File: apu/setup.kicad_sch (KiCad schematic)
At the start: 22 parts, among them U1 X818336-001

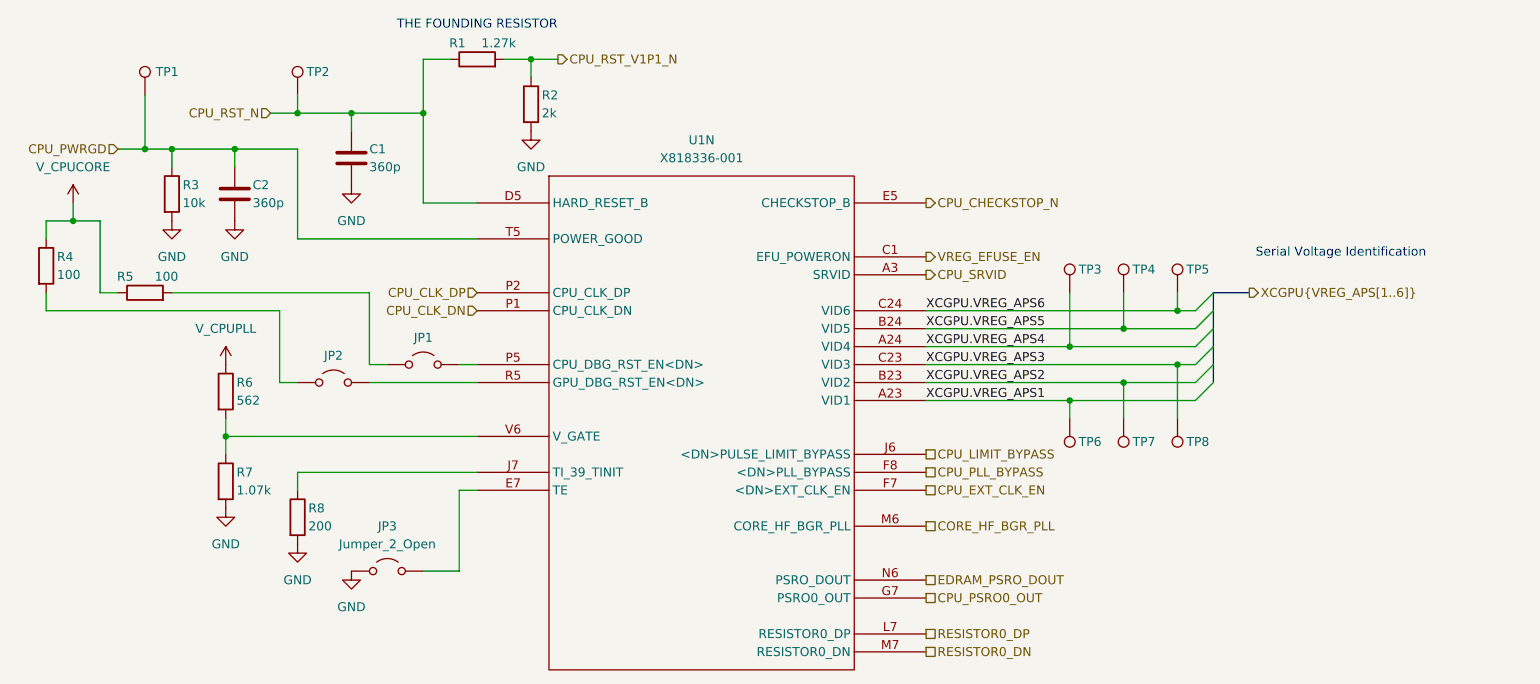
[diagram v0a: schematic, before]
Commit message: Cleanup, SMC GPIO connections and Temperature sensing
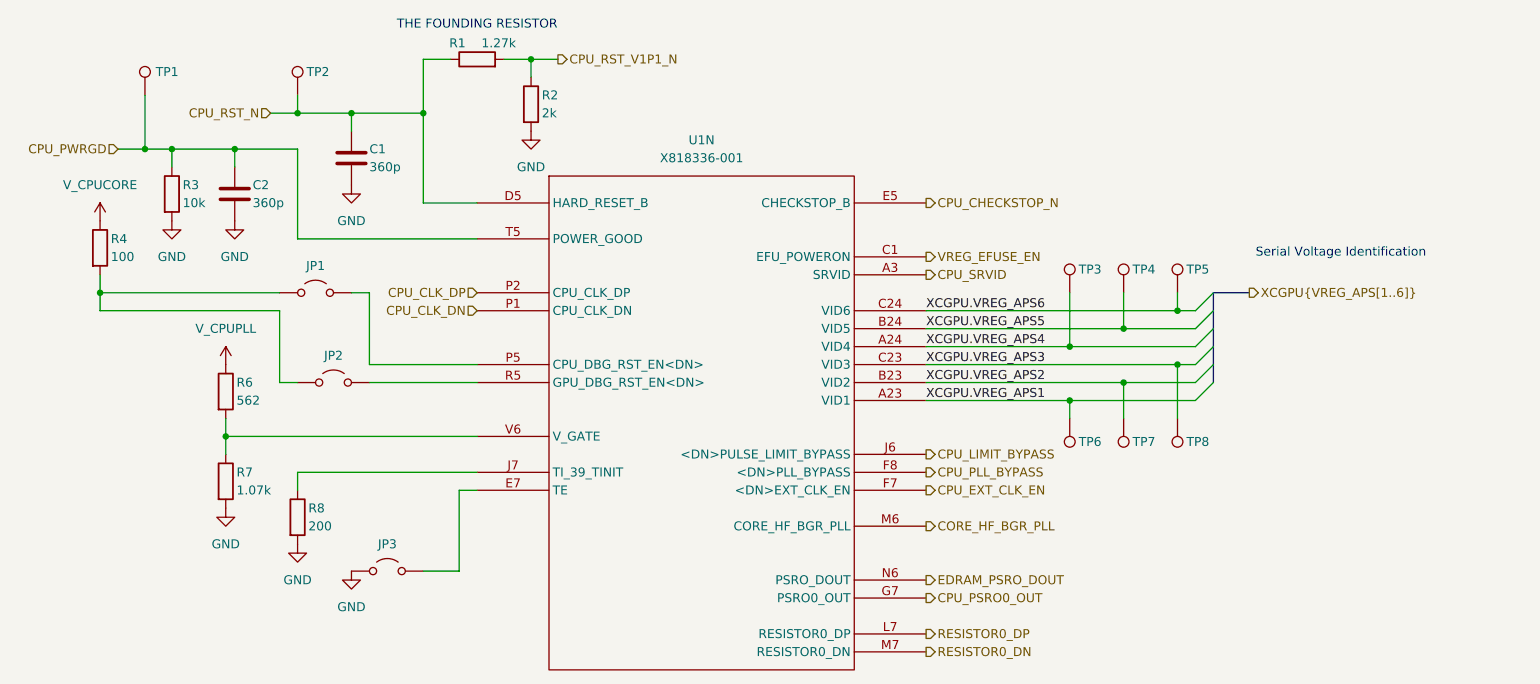
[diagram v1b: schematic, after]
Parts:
- removed R5: 100, symbol Device:R
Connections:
- net at JP2.1 (A), R4.2: now also JP1.1 (A)
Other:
- moved on the sheet: JP1, R4

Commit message: Internal Connectors
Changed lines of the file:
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@@
 	(text "Serial Voltage Identification\n"
 		(exclude_from_sim no)
-		(at 240.284 70.612 0)
+		(at 237.744 72.644 0)
 		(effects
 			(font
@@
 	(bus
 		(pts
-			(xy 222.25 76.2) (xy 227.33 76.2)
+			(xy 222.25 76.2) (xy 224.79 76.2)
 		)
 		(stroke
@@
 	(hierarchical_label "XCGPU{VREG_APS[1..6]}"
 		(shape output)
-		(at 227.33 76.2 0)
-		(effects
-			(font
+		(at 224.79 76.2 0)
+		(effects
+			(font

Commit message: Cleanup & Debug I/O
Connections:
- net V_CPUPLL renamed +1.8V
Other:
- note added: "VID (Voltage Identification Definition)"
- note removed: "Serial Voltage Identification"
- moved on the sheet: C2, JP3, R2, TP1

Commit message: Debug Connectors
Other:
- moved on the sheet: JP1
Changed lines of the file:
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@@
 	)
 	(junction
-		(at 64.77 76.2)
-		(diameter 0)
-		(color 0 0 0 0)
-	)
-	(junction
 		(at 85.09 55.88)
 		(diameter 0)
@@
 	)
 	(junction
+		(at 90.17 81.28)
+		(diameter 0)
+		(color 0 0 0 0)
+	)
+	(junction
 		(at 92.71 50.8)
 		(diameter 0)
@@
 	(wire
 		(pts
-			(xy 64.77 73.66) (xy 64.77 76.2)
+			(xy 64.77 73.66) (xy 64.77 78.74)
 		)
 		(stroke
@@
 	(wire
 		(pts
-			(xy 100.33 76.2) (xy 102.87 76.2)
+			(xy 92.71 101.6) (xy 92.71 104.14)
 		)
 		(stroke
@@
 	(wire
 		(pts
-			(xy 92.71 101.6) (xy 92.71 104.14)
+			(xy 100.33 50.8) (xy 110.49 50.8)
 		)
 		(stroke
@@
 	(wire
 		(pts
-			(xy 100.33 50.8) (xy 110.49 50.8)
+			(xy 74.93 55.88) (xy 85.09 55.88)
 		)
 		(stroke
@@
 	(wire
 		(pts
-			(xy 74.93 55.88) (xy 85.09 55.88)
+			(xy 85.09 55.88) (xy 85.09 58.42)
 		)
 		(stroke
@@
 	(wire
 		(pts
-			(xy 85.09 55.88) (xy 85.09 58.42)
+			(xy 85.09 55.88) (xy 95.25 55.88)
 		)
 		(stroke
@@
 	(wire
 		(pts
-			(xy 102.87 76.2) (xy 102.87 86.36)
+			(xy 82.55 93.98) (xy 82.55 96.52)
 		)
 		(stroke
@@
 	(wire
 		(pts
-			(xy 85.09 55.88) (xy 95.25 55.88)
+			(xy 209.55 81.28) (xy 219.71 81.28)
 		)
 		(stroke
@@
 	(wire
 		(pts
-			(xy 82.55 93.98) (xy 82.55 96.52)
+			(xy 92.71 50.8) (xy 100.33 50.8)
 		)
 		(stroke
@@
 	(wire
 		(pts
-			(xy 209.55 81.28) (xy 219.71 81.28)
+			(xy 90.17 81.28) (xy 90.17 88.9)
 		)
 		(stroke
@@
 	(wire
 		(pts
-			(xy 92.71 50.8) (xy 100.33 50.8)
+			(xy 74.93 50.8) (xy 74.93 55.88)
 		)
 		(stroke
@@
 	(wire
 		(pts
-			(xy 74.93 50.8) (xy 74.93 55.88)
+			(xy 102.87 81.28) (xy 105.41 81.28)
 		)
 		(stroke
@@
 	(wire
 		(pts
-			(xy 102.87 86.36) (xy 118.11 86.36)
+			(xy 105.41 81.28) (xy 105.41 86.36)
 		)
 		(stroke
@@
 	(wire
 		(pts
-			(xy 92.71 88.9) (xy 90.17 88.9)
+			(xy 105.41 86.36) (xy 118.11 86.36)
 		)
 		(stroke
@@
 	(wire
 		(pts
-			(xy 219.71 86.36) (xy 217.17 86.36)
+			(xy 92.71 88.9) (xy 90.17 88.9)
 		)
 		(stroke
@@
 	(wire
 		(pts
-			(xy 110.49 43.18) (xy 114.3 43.18)
+			(xy 219.71 86.36) (xy 217.17 86.36)
 		)
 		(stroke
@@
 	(wire
 		(pts
-			(xy 64.77 76.2) (xy 90.17 76.2)
+			(xy 110.49 43.18) (xy 114.3 43.18)
 		)
 		(stroke
@@
 	(wire
 		(pts
-			(xy 90.17 78.74) (xy 90.17 88.9)
+			(xy 90.17 78.74) (xy 90.17 81.28)
 		)
 		(stroke
@@
 	(wire
 		(pts
+			(xy 90.17 81.28) (xy 92.71 81.28)
+		)
+		(stroke
+			(width 0)
+			(type default)
+		)
+	)
+	(wire
+		(pts
 			(xy 219.71 78.74) (xy 217.17 78.74)
 		)
@@
 	(wire
 		(pts
-			(xy 64.77 76.2) (xy 64.77 78.74)
-		)
-		(stroke
-			(width 0)
-			(type default)
-		)
-	)
-	(wire
-		(pts
 			(xy 82.55 96.52) (xy 82.55 99.06)
 		)
@@
 	(symbol
 		(lib_id "Jumper:Jumper_2_Open")
-		(at 95.25 76.2 0)
+		(at 97.79 81.28 0)
 		(unit 1)
 		(exclude_from_sim no)
@@
 		(dnp no)
 		(property "Reference" "JP1"
-			(at 95.25 72.39 0)
+			(at 97.79 77.47 0)
 			(effects
 				(font
@@
 		)
 		(property "Value" "Jumper_2_Open"
-			(at 95.25 72.39 0)
+			(at 97.79 77.47 0)
 			(effects
 				(font
@@
 		)
 		(property "Footprint" ""
-			(at 95.25 76.2 0)
+			(at 97.79 81.28 0)
 			(effects
 				(font
@@
 		)
 		(property "Datasheet" "~"
-			(at 95.25 76.2 0)
+			(at 97.79 81.28 0)
 			(effects
 				(font
@@
 		)
 		(property "Description" "Jumper, 2-pole, open"
-			(at 95.25 76.2 0)
+			(at 97.79 81.28 0)
 			(effects
 				(font

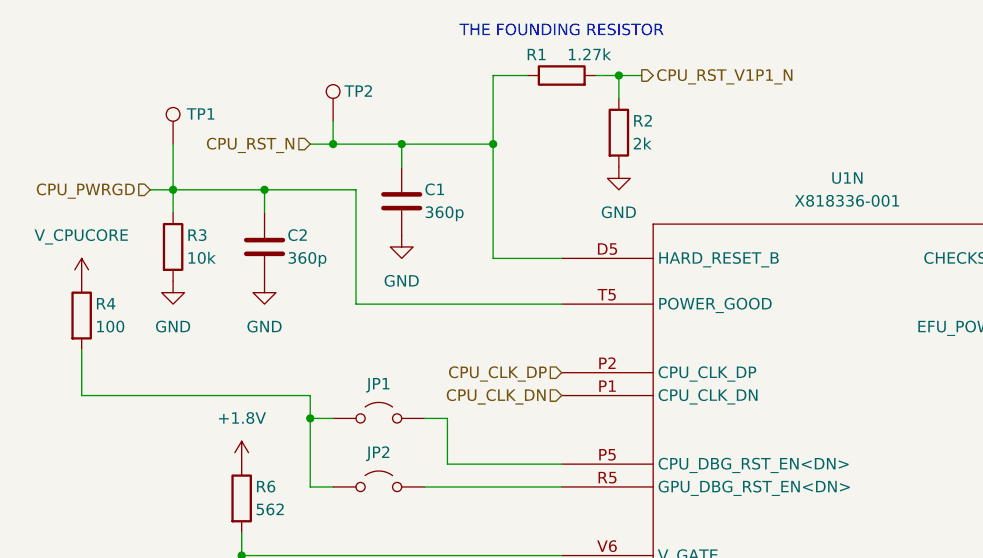
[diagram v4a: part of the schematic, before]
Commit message: Nand Flash, Sata Connectors and removing (hopefully) unnecessary things
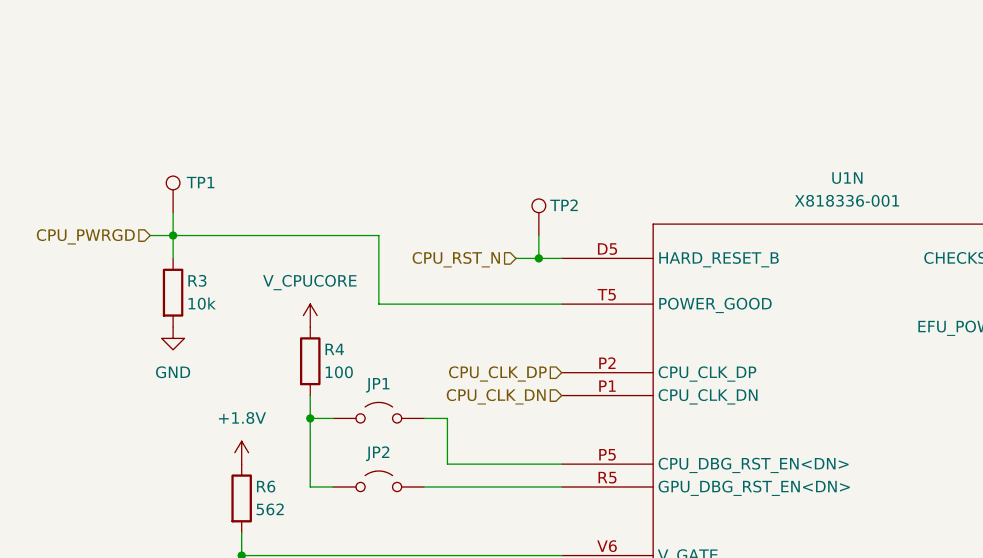
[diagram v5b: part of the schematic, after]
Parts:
- removed C1, C2: 360p, symbol Device:C
- removed R1: 1.27k, symbol Device:R
- removed R2: 2k, symbol Device:R
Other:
- note removed: "THE FOUNDING RESISTOR"
- moved on the sheet: R3, R4, TP1, TP2

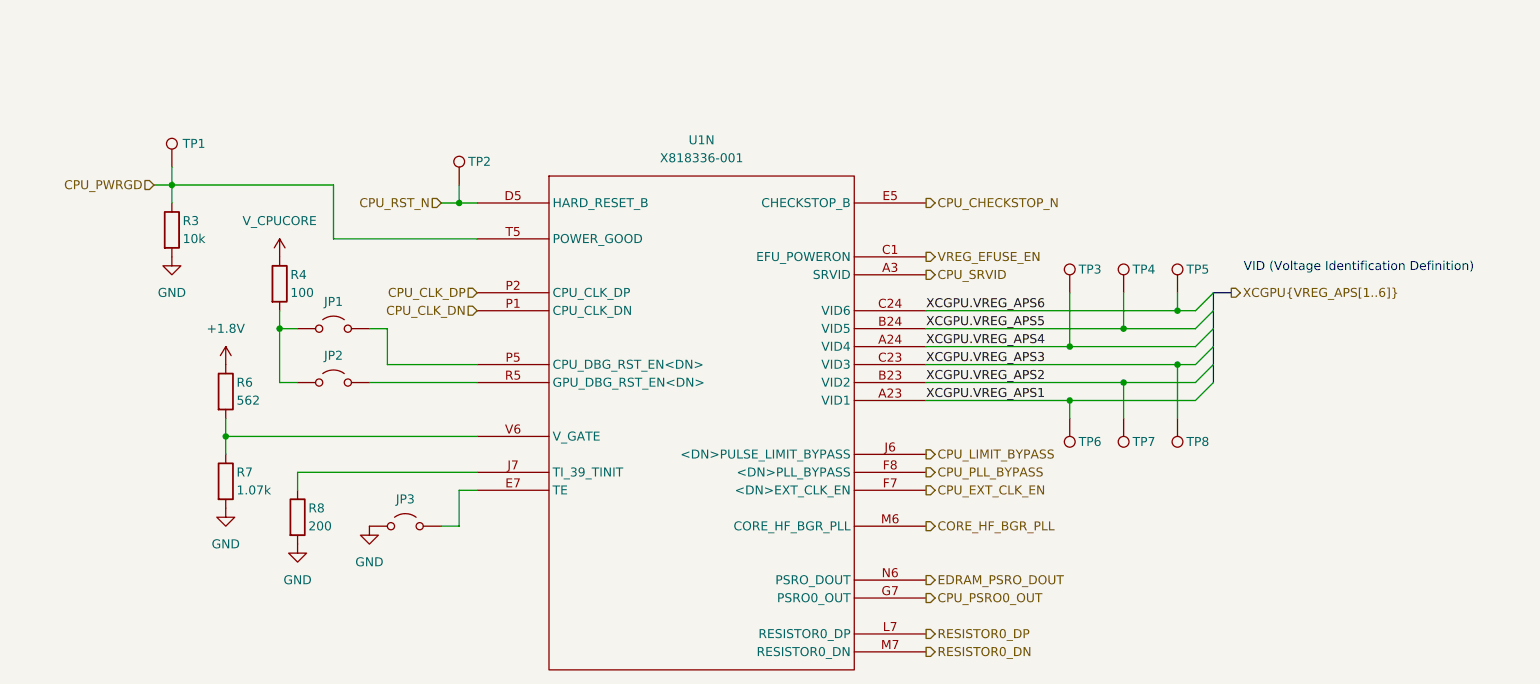
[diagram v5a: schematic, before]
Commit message: Multipurpose and standby power rails, Reannotated schematic
Added V_1P2, V_1P8, V_5P0DUAL, V_EFUSE, V_GPUPCIE, V_3P3STBY and V_1P2STBY
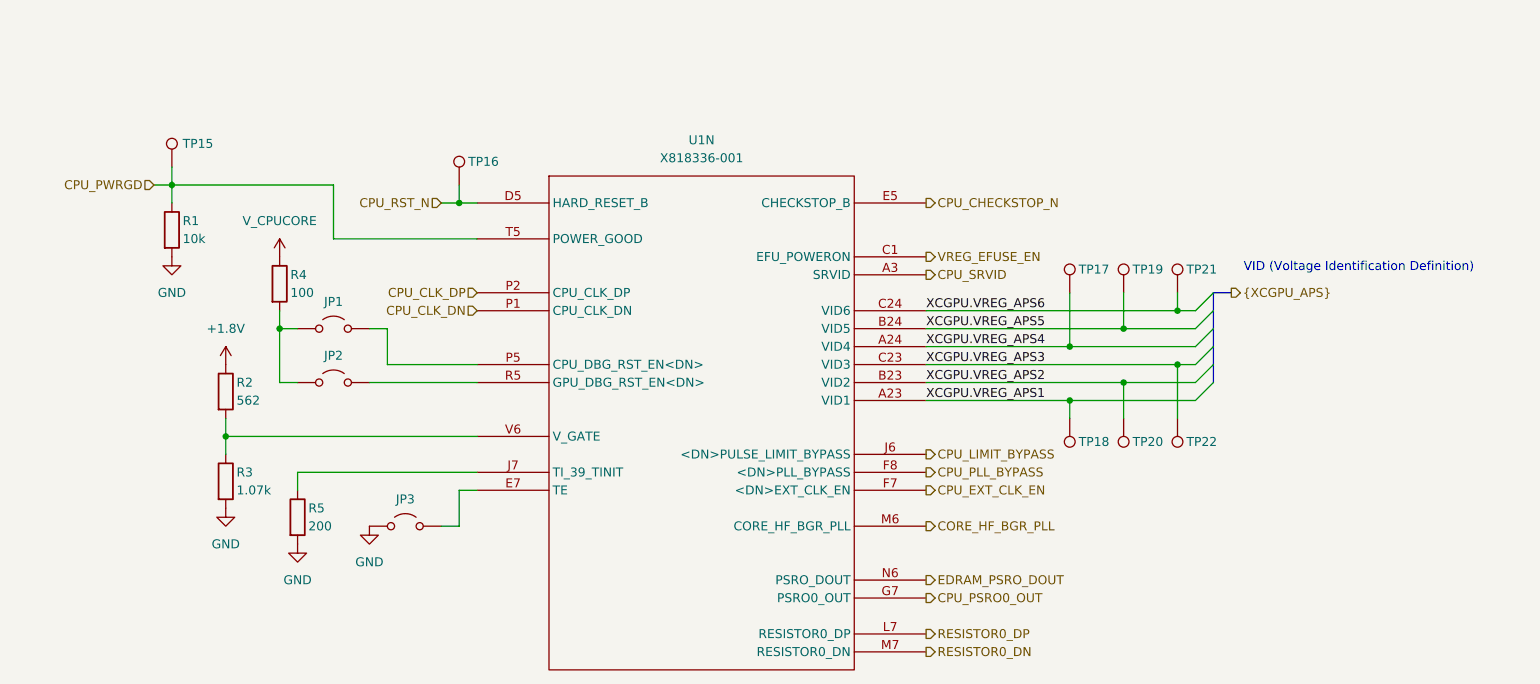
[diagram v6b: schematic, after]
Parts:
- renumbered R3 to R1, R6 to R2, R7 to R3, R8 to R5, TP1 to TP15, TP2 to TP16, TP3 to TP17, TP6 to TP18, TP4 to TP19, TP7 to TP20, TP5 to TP21, TP8 to TP22
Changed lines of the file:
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@@
 		)
 	)
-	(hierarchical_label "XCGPU{VREG_APS[1..6]}"
+	(hierarchical_label "{XCGPU_APS}"
 		(shape output)
 		(at 224.79 76.2 0)
@@
 		(on_board yes)
 		(dnp no)
-		(property "Reference" "TP2"
+		(property "Reference" "TP16"
 			(at 116.84 57.658 0)
 			(effects
@@
 			(project "StingBurst"
 				(path "/16640ecb-e4a4-4594-871b-70047bfba6e0/15d9acf0-ed9b-44aa-a266-2c44722c6abb/ae60d6be-3587-4435-b525-992ac09fdec2"
-					(reference "TP2")
+					(reference "TP16")
 					(unit 1)
 				)
@@
 		(on_board yes)
 		(dnp no)
-		(property "Reference" "TP5"
+		(property "Reference" "TP21"
 			(at 218.44 72.898 0)
 			(effects
@@
 			(project "StingBurst"
 				(path "/16640ecb-e4a4-4594-871b-70047bfba6e0/15d9acf0-ed9b-44aa-a266-2c44722c6abb/ae60d6be-3587-4435-b525-992ac09fdec2"
-					(reference "TP5")
+					(reference "TP21")
 					(unit 1)
 				)
@@
 		(on_board yes)
 		(dnp no)
-		(property "Reference" "R6"
+		(property "Reference" "R2"
 			(at 84.074 88.9 0)
 			(effects
@@
 			(project "StingBurst"
 				(path "/16640ecb-e4a4-4594-871b-70047bfba6e0/15d9acf0-ed9b-44aa-a266-2c44722c6abb/ae60d6be-3587-4435-b525-992ac09fdec2"
-					(reference "R6")
+					(reference "R2")
 					(unit 1)
 				)
@@
 		(on_board yes)
 		(dnp no)
-		(property "Reference" "R7"
+		(property "Reference" "R3"
 			(at 84.074 101.6 0)
 			(effects
@@
 			(project "StingBurst"
 				(path "/16640ecb-e4a4-4594-871b-70047bfba6e0/15d9acf0-ed9b-44aa-a266-2c44722c6abb/ae60d6be-3587-4435-b525-992ac09fdec2"
-					(reference "R7")
+					(reference "R3")
 					(unit 1)
 				)
@@
 		(on_board yes)
 		(dnp no)
-		(property "Reference" "R8"
+		(property "Reference" "R5"
 			(at 94.234 106.68 0)
 			(effects
@@
 			(project "StingBurst"
 				(path "/16640ecb-e4a4-4594-871b-70047bfba6e0/15d9acf0-ed9b-44aa-a266-2c44722c6abb/ae60d6be-3587-4435-b525-992ac09fdec2"
-					(reference "R8")
+					(reference "R5")
 					(unit 1)
 				)
@@
 		(on_board yes)
 		(dnp no)
-		(property "Reference" "TP6"
+		(property "Reference" "TP18"
 			(at 203.2 97.282 0)
 			(effects
@@
 			(project "StingBurst"
 				(path "/16640ecb-e4a4-4594-871b-70047bfba6e0/15d9acf0-ed9b-44aa-a266-2c44722c6abb/ae60d6be-3587-4435-b525-992ac09fdec2"
-					(reference "TP6")
+					(reference "TP18")
 					(unit 1)
 				)
@@
 		(on_board yes)
 		(dnp no)
-		(property "Reference" "TP7"
+		(property "Reference" "TP20"
 			(at 210.82 97.282 0)
 			(effects
@@
 			(project "StingBurst"
 				(path "/16640ecb-e4a4-4594-871b-70047bfba6e0/15d9acf0-ed9b-44aa-a266-2c44722c6abb/ae60d6be-3587-4435-b525-992ac09fdec2"
-					(reference "TP7")
+					(reference "TP20")
 					(unit 1)
 				)
@@
 		(on_board yes)
 		(dnp no)
-		(property "Reference" "TP4"
+		(property "Reference" "TP19"
 			(at 210.82 72.898 0)
 			(effects
@@
 			(project "StingBurst"
 				(path "/16640ecb-e4a4-4594-871b-70047bfba6e0/15d9acf0-ed9b-44aa-a266-2c44722c6abb/ae60d6be-3587-4435-b525-992ac09fdec2"
-					(reference "TP4")
+					(reference "TP19")
 					(unit 1)
 				)
@@
 		(dnp no)
 		(fields_autoplaced yes)
-		(property "Reference" "#PWR06"
+		(property "Reference" "#PWR02"
 			(at 82.55 90.17 0)
 			(effects
@@
 			(project "Mantaray"
 				(path "/16640ecb-e4a4-4594-871b-70047bfba6e0/15d9acf0-ed9b-44aa-a266-2c44722c6abb/ae60d6be-3587-4435-b525-992ac09fdec2"
-					(reference "#PWR06")
+					(reference "#PWR02")
 					(unit 1)
 				)
@@
 		(dnp no)
 		(fields_autoplaced yes)
-		(property "Reference" "#PWR08"
+		(property "Reference" "#PWR05"
 			(at 92.71 118.11 0)
 			(effects
@@
 			(project "StingBurst"
 				(path "/16640ecb-e4a4-4594-871b-70047bfba6e0/15d9acf0-ed9b-44aa-a266-2c44722c6abb/ae60d6be-3587-4435-b525-992ac09fdec2"
-					(reference "#PWR08")
+					(reference "#PWR05")
 					(unit 1)
 				)
@@
 		(on_board yes)
 		(dnp no)
-		(property "Reference" "TP3"
+		(property "Reference" "TP17"
 			(at 203.2 72.898 0)
 			(effects
@@
 			(project "StingBurst"
 				(path "/16640ecb-e4a4-4594-871b-70047bfba6e0/15d9acf0-ed9b-44aa-a266-2c44722c6abb/ae60d6be-3587-4435-b525-992ac09fdec2"
-					(reference "TP3")
+					(reference "TP17")
 					(unit 1)
 				)
@@
 		(dnp no)
 		(fields_autoplaced yes)
-		(property "Reference" "#PWR07"
+		(property "Reference" "#PWR03"
 			(at 82.55 113.03 0)
 			(effects
@@
 			(project "StingBurst"
 				(path "/16640ecb-e4a4-4594-871b-70047bfba6e0/15d9acf0-ed9b-44aa-a266-2c44722c6abb/ae60d6be-3587-4435-b525-992ac09fdec2"
-					(reference "#PWR07")
+					(reference "#PWR03")
 					(unit 1)
 				)
@@
 		(on_board yes)
 		(dnp no)
-		(property "Reference" "#PWR03"
+		(property "Reference" "#PWR04"
 			(at 90.17 74.93 0)
 			(effects
@@
 			(project "StingBurst"
 				(path "/16640ecb-e4a4-4594-871b-70047bfba6e0/15d9acf0-ed9b-44aa-a266-2c44722c6abb/ae60d6be-3587-4435-b525-992ac09fdec2"
-					(reference "#PWR03")
+					(reference "#PWR04")
 					(unit 1)
 				)
@@
 		(on_board yes)
 		(dnp no)
-		(property "Reference" "TP8"
+		(property "Reference" "TP22"
 			(at 218.44 97.282 0)
 			(effects
@@
 			(project "StingBurst"
 				(path "/16640ecb-e4a4-4594-871b-70047bfba6e0/15d9acf0-ed9b-44aa-a266-2c44722c6abb/ae60d6be-3587-4435-b525-992ac09fdec2"
-					(reference "TP8")
+					(reference "TP22")
 					(unit 1)
 				)
@@
 		(on_board yes)
 		(dnp no)
-		(property "Reference" "TP1"
+		(property "Reference" "TP15"
 			(at 76.454 55.118 0)
 			(effects
@@
 			(project "StingBurst"
 				(path "/16640ecb-e4a4-4594-871b-70047bfba6e0/15d9acf0-ed9b-44aa-a266-2c44722c6abb/ae60d6be-3587-4435-b525-992ac09fdec2"
-					(reference "TP1")
+					(reference "TP15")
 					(unit 1)
 				)
@@
 		(dnp no)
 		(fields_autoplaced yes)
-		(property "Reference" "#PWR09"
+		(property "Reference" "#PWR06"
 			(at 102.87 115.57 0)
 			(effects
@@
 			(project "StingBurst"
 				(path "/16640ecb-e4a4-4594-871b-70047bfba6e0/15d9acf0-ed9b-44aa-a266-2c44722c6abb/ae60d6be-3587-4435-b525-992ac09fdec2"
-					(reference "#PWR09")
+					(reference "#PWR06")
 					(unit 1)
 				)
@@
 		(on_board yes)
 		(dnp no)
-		(property "Reference" "R3"
+		(property "Reference" "R1"
 			(at 76.454 66.04 0)
 			(effects
@@
 			(project "StingBurst"
 				(path "/16640ecb-e4a4-4594-871b-70047bfba6e0/15d9acf0-ed9b-44aa-a266-2c44722c6abb/ae60d6be-3587-4435-b525-992ac09fdec2"
-					(reference "R3")
+					(reference "R1")
 					(unit 1)
 				)
@@
 		(dnp no)
 		(fields_autoplaced yes)
-		(property "Reference" "#PWR04"
+		(property "Reference" "#PWR01"
 			(at 74.93 77.47 0)
 			(effects
@@
 			(project "StingBurst"
 				(path "/16640ecb-e4a4-4594-871b-70047bfba6e0/15d9acf0-ed9b-44aa-a266-2c44722c6abb/ae60d6be-3587-4435-b525-992ac09fdec2"
-					(reference "#PWR04")
+					(reference "#PWR01")
 					(unit 1)
 				)
